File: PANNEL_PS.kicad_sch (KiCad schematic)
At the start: 24 parts, among them IC30 TPS25940ARVCR, IC31 INA226AIDGSR

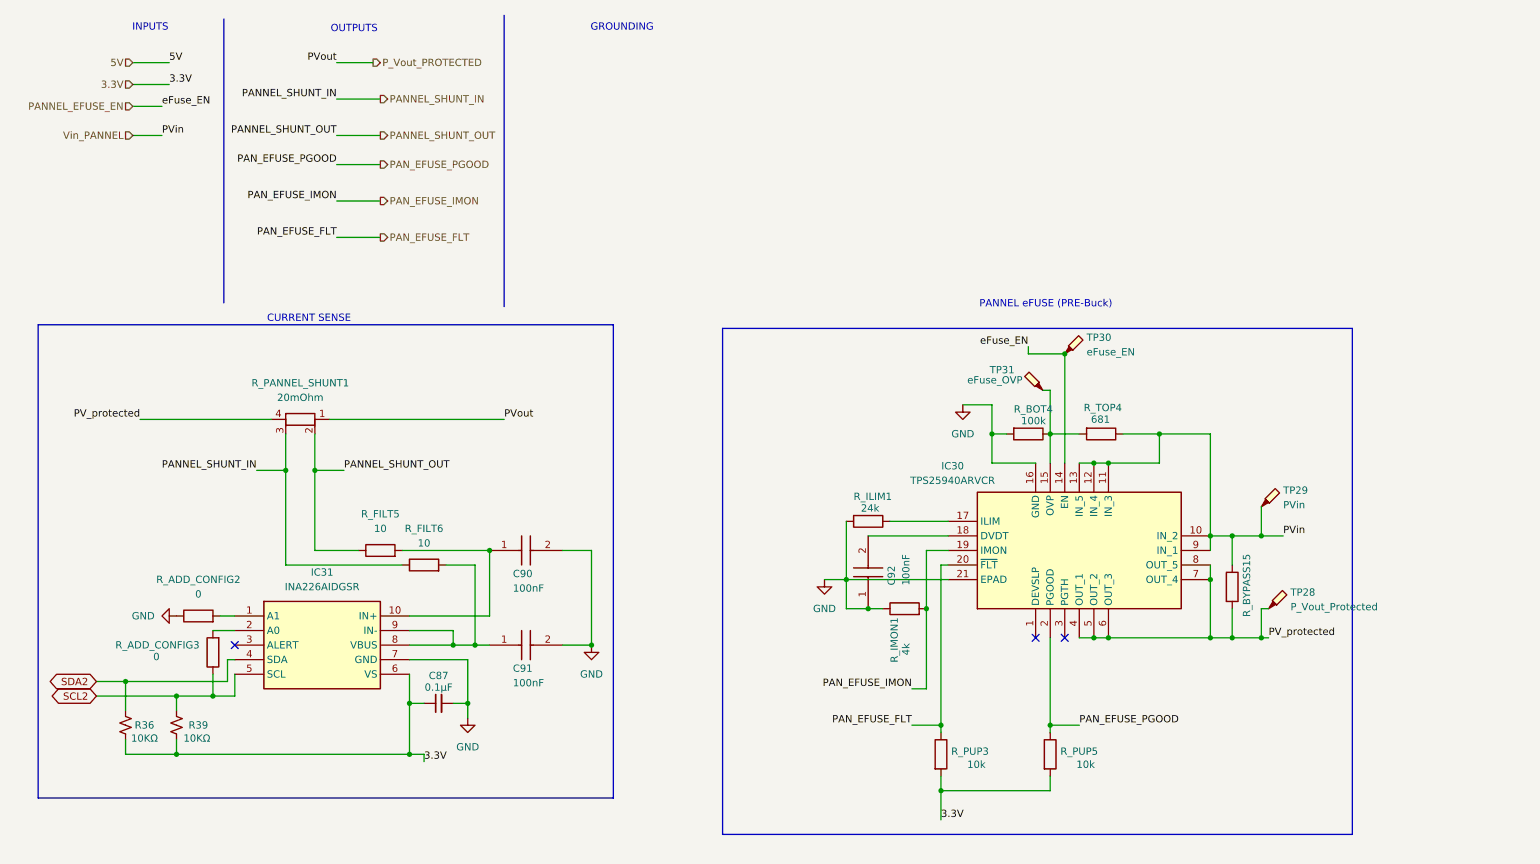
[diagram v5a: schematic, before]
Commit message: changed mcu power suppl
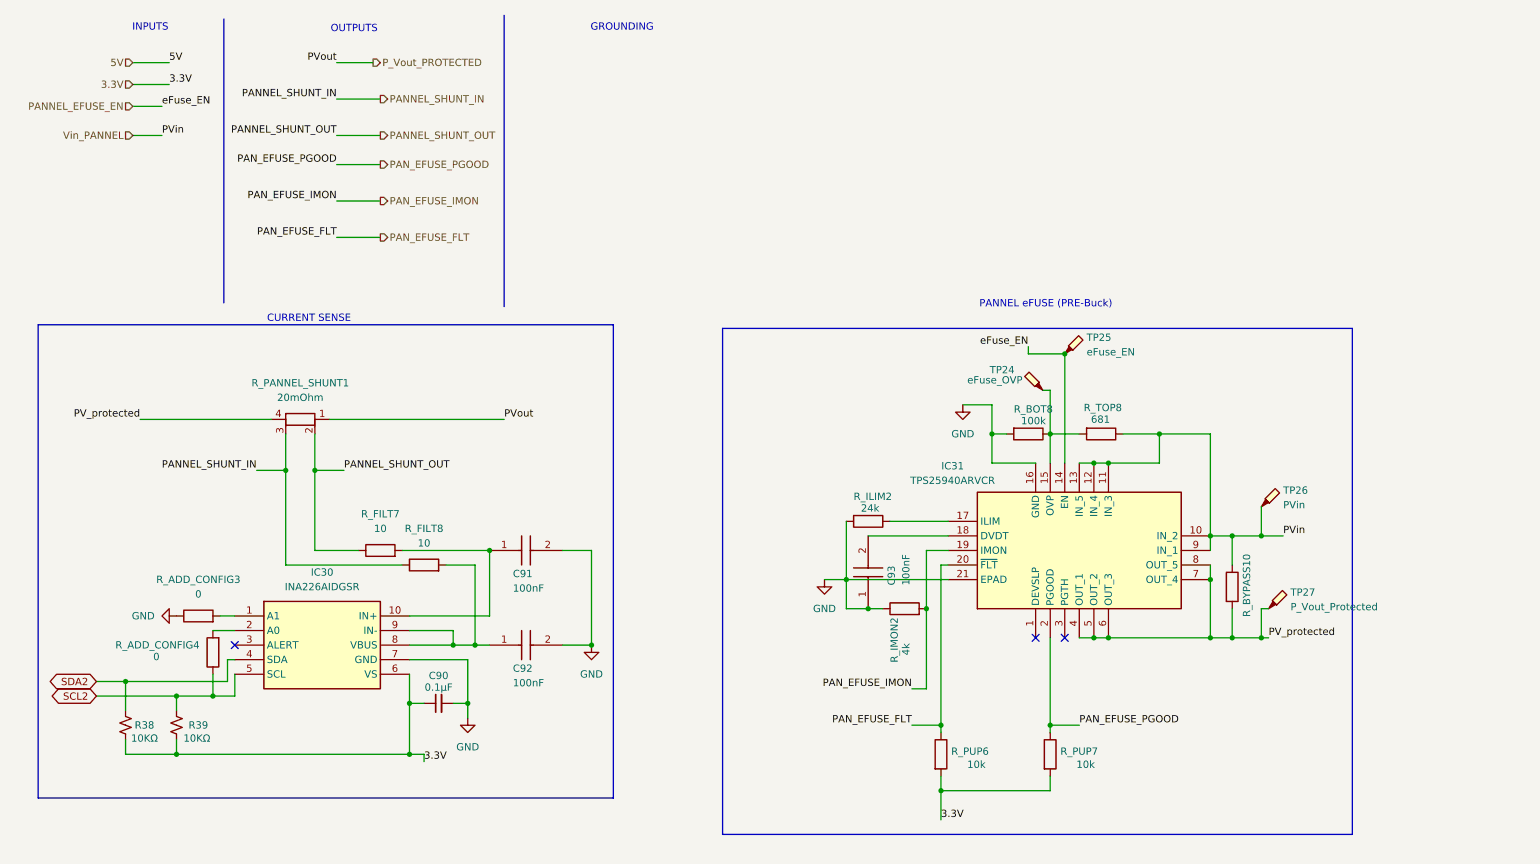
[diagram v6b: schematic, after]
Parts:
- renumbered C87 to C90, C90 to C91, C91 to C92, C92 to C93, IC31 to IC30, IC30 to IC31, R36 to R38, R_ADD_CONFIG2 to R_ADD_CONFIG3, R_ADD_CONFIG3 to R_ADD_CONFIG4, R_BOT4 to R_BOT8, R_BYPASS15 to R_BYPASS10, R_FILT5 to R_FILT7, R_FILT6 to R_FILT8, R_ILIM1 to R_ILIM2, R_IMON1 to R_IMON2, R_PUP3 to R_PUP6, R_PUP5 to R_PUP7, R_TOP4 to R_TOP8, TP31 to TP24, TP30 to TP25, TP29 to TP26, TP28 to TP27
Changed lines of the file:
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@@
 		(dnp no)
 		(fields_autoplaced yes)
-		(property "Reference" "IC31"
+		(property "Reference" "IC30"
 			(at 66.04 111.76 0)
 			(effects
@@
 			(project "PULSE_ENG"
 				(path "/2de881bb-2e2a-47f9-96ed-b3393fa36b98/c72bc6ca-9cdc-4e58-ad5e-fa33c03e7ecd"
-					(reference "IC31")
+					(reference "IC30")
 					(unit 1)
 				)
@@
 		(dnp no)
 		(fields_autoplaced yes)
-		(property "Reference" "#PWR025"
+		(property "Reference" "#PWR070"
 			(at 177.8 88.9 0)
 			(effects
@@
 			(project "PULSE_ENG"
 				(path "/2de881bb-2e2a-47f9-96ed-b3393fa36b98/c72bc6ca-9cdc-4e58-ad5e-fa33c03e7ecd"
-					(reference "#PWR025")
+					(reference "#PWR070")
 					(unit 1)
 				)
@@
 		(on_board yes)
 		(dnp no)
-		(property "Reference" "R_BOT4"
+		(property "Reference" "R_BOT8"
 			(at 186.69 83.312 90)
 			(effects
@@
 			(project "PULSE_ENG"
 				(path "/2de881bb-2e2a-47f9-96ed-b3393fa36b98/c72bc6ca-9cdc-4e58-ad5e-fa33c03e7ecd"
-					(reference "R_BOT4")
+					(reference "R_BOT8")
 					(unit 1)
 				)
@@
 		(on_board yes)
 		(dnp no)
-		(property "Reference" "R_PUP5"
+		(property "Reference" "R_PUP7"
 			(at 194.818 143.002 0)
 			(effects
@@
 			(project "PULSE_ENG"
 				(path "/2de881bb-2e2a-47f9-96ed-b3393fa36b98/c72bc6ca-9cdc-4e58-ad5e-fa33c03e7ecd"
-					(reference "R_PUP5")
+					(reference "R_PUP7")
 					(unit 1)
 				)
@@
 		(dnp no)
 		(fields_autoplaced yes)
-		(property "Reference" "#PWR024"
+		(property "Reference" "#PWR069"
 			(at 153.67 119.38 0)
 			(effects
@@
 			(project "PULSE_ENG"
 				(path "/2de881bb-2e2a-47f9-96ed-b3393fa36b98/c72bc6ca-9cdc-4e58-ad5e-fa33c03e7ecd"
-					(reference "#PWR024")
+					(reference "#PWR069")
 					(unit 1)
 				)
@@
 		(on_board yes)
 		(dnp no)
-		(property "Reference" "R_ILIM1"
+		(property "Reference" "R_ILIM2"
 			(at 158.75 98.552 90)
 			(effects
@@
 			(project "PULSE_ENG"
 				(path "/2de881bb-2e2a-47f9-96ed-b3393fa36b98/c72bc6ca-9cdc-4e58-ad5e-fa33c03e7ecd"
-					(reference "R_ILIM1")
+					(reference "R_ILIM2")
 					(unit 1)
 				)
@@
 		(dnp no)
 		(fields_autoplaced yes)
-		(property "Reference" "R_FILT6"
+		(property "Reference" "R_FILT8"
 			(at 83.82 104.14 90)
 			(effects
@@
 			(project "PULSE_ENG"
 				(path "/2de881bb-2e2a-47f9-96ed-b3393fa36b98/c72bc6ca-9cdc-4e58-ad5e-fa33c03e7ecd"
-					(reference "R_FILT6")
+					(reference "R_FILT8")
 					(unit 1)
 				)
@@
 		(on_board yes)
 		(dnp no)
-		(property "Reference" "IC30"
+		(property "Reference" "IC31"
 			(at 176.022 93.218 90)
 			(effects
@@
 			(project "PULSE_ENG"
 				(path "/2de881bb-2e2a-47f9-96ed-b3393fa36b98/c72bc6ca-9cdc-4e58-ad5e-fa33c03e7ecd"
-					(reference "IC30")
+					(reference "IC31")
 					(unit 1)
 				)
@@
 		(dnp no)
 		(fields_autoplaced yes)
-		(property "Reference" "R_FILT5"
+		(property "Reference" "R_FILT7"
 			(at 76.2 101.6 90)
 			(effects
@@
 			(project "PULSE_ENG"
 				(path "/2de881bb-2e2a-47f9-96ed-b3393fa36b98/c72bc6ca-9cdc-4e58-ad5e-fa33c03e7ecd"
-					(reference "R_FILT5")
+					(reference "R_FILT7")
 					(unit 1)
 				)
@@
 		(on_board yes)
 		(dnp no)
-		(property "Reference" "R_TOP4"
+		(property "Reference" "R_TOP8"
 			(at 198.882 83.058 90)
 			(effects
@@
 			(project "PULSE_ENG"
 				(path "/2de881bb-2e2a-47f9-96ed-b3393fa36b98/c72bc6ca-9cdc-4e58-ad5e-fa33c03e7ecd"
-					(reference "R_TOP4")
+					(reference "R_TOP8")
 					(unit 1)
 				)
@@
 		(on_board yes)
 		(dnp no)
-		(property "Reference" "TP31"
+		(property "Reference" "TP24"
 			(at 184.658 76.454 90)
 			(effects
@@
 			(project "PULSE_ENG"
 				(path "/2de881bb-2e2a-47f9-96ed-b3393fa36b98/c72bc6ca-9cdc-4e58-ad5e-fa33c03e7ecd"
-					(reference "TP31")
+					(reference "TP24")
 					(unit 1)
 				)
@@
 		(dnp no)
 		(fields_autoplaced yes)
-		(property "Reference" "#PWR021"
+		(property "Reference" "#PWR068"
 			(at 113.03 130.81 0)
 			(effects
@@
 			(project "PULSE_ENG"
 				(path "/2de881bb-2e2a-47f9-96ed-b3393fa36b98/c72bc6ca-9cdc-4e58-ad5e-fa33c03e7ecd"
-					(reference "#PWR021")
+					(reference "#PWR068")
 					(unit 1)
 				)
@@
 		(dnp no)
 		(fields_autoplaced yes)
-		(property "Reference" "TP29"
+		(property "Reference" "TP26"
 			(at 233.68 97.4724 0)
 			(effects
@@
 			(project "PULSE_ENG"
 				(path "/2de881bb-2e2a-47f9-96ed-b3393fa36b98/c72bc6ca-9cdc-4e58-ad5e-fa33c03e7ecd"
-					(reference "TP29")
+					(reference "TP26")
 					(unit 1)
 				)
@@
 		(dnp no)
 		(fields_autoplaced yes)
-		(property "Reference" "#PWR020"
+		(property "Reference" "#PWR067"
 			(at 91.44 143.51 0)
 			(effects
@@
 			(project "PULSE_ENG"
 				(path "/2de881bb-2e2a-47f9-96ed-b3393fa36b98/c72bc6ca-9cdc-4e58-ad5e-fa33c03e7ecd"
-					(reference "#PWR020")
+					(reference "#PWR067")
 					(unit 1)
 				)
@@
 		(on_board yes)
 		(dnp no)
-		(property "Reference" "R_PUP3"
+		(property "Reference" "R_PUP6"
 			(at 175.768 143.002 0)
 			(effects
@@
 			(project "PULSE_ENG"
 				(path "/2de881bb-2e2a-47f9-96ed-b3393fa36b98/c72bc6ca-9cdc-4e58-ad5e-fa33c03e7ecd"
-					(reference "R_PUP3")
+					(reference "R_PUP6")
 					(unit 1)
 				)
@@
 		(dnp no)
 		(fields_autoplaced yes)
-		(property "Reference" "#PWR019"
+		(property "Reference" "#PWR066"
 			(at 34.29 119.38 0)
 			(effects
@@
 			(project "PULSE_ENG"
 				(path "/2de881bb-2e2a-47f9-96ed-b3393fa36b98/c72bc6ca-9cdc-4e58-ad5e-fa33c03e7ecd"
-					(reference "#PWR019")
+					(reference "#PWR066")
 					(unit 1)
 				)
@@
 		(on_board yes)
 		(dnp no)
-		(property "Reference" "C90"
+		(property "Reference" "C91"
 			(at 99.314 112.014 0)
 			(effects
@@
 			(project "PULSE_ENG"
 				(path "/2de881bb-2e2a-47f9-96ed-b3393fa36b98/c72bc6ca-9cdc-4e58-ad5e-fa33c03e7ecd"
-					(reference "C90")
+					(reference "C91")
 					(unit 1)
 				)
@@
 		(dnp no)
 		(fields_autoplaced yes)
-		(property "Reference" "TP28"
+		(property "Reference" "TP27"
 			(at 234.95 115.2524 0)
 			(effects
@@
 			(project "PULSE_ENG"
 				(path "/2de881bb-2e2a-47f9-96ed-b3393fa36b98/c72bc6ca-9cdc-4e58-ad5e-fa33c03e7ecd"
-					(reference "TP28")
+					(reference "TP27")
 					(unit 1)
 				)
@@
 		(on_board yes)
 		(dnp no)
-		(property "Reference" "R_ADD_CONFIG3"
+		(property "Reference" "R_ADD_CONFIG4"
 			(at 29.972 124.46 0)
 			(effects
@@
 			(project "PULSE_ENG"
 				(path "/2de881bb-2e2a-47f9-96ed-b3393fa36b98/c72bc6ca-9cdc-4e58-ad5e-fa33c03e7ecd"
-					(reference "R_ADD_CONFIG3")
+					(reference "R_ADD_CONFIG4")
 					(unit 1)
 				)
@@
 		(on_board yes)
 		(dnp no)
-		(property "Reference" "C91"
+		(property "Reference" "C92"
 			(at 99.314 128.524 0)
 			(effects
@@
 			(project "PULSE_ENG"
 				(path "/2de881bb-2e2a-47f9-96ed-b3393fa36b98/c72bc6ca-9cdc-4e58-ad5e-fa33c03e7ecd"
-					(reference "C91")
+					(reference "C92")
 					(unit 1)
 				)
@@
 		(on_board yes)
 		(dnp no)
-		(property "Reference" "C92"
+		(property "Reference" "C93"
 			(at 165.354 114.046 0)
 			(effects
@@
 			(project "PULSE_ENG"
 				(path "/2de881bb-2e2a-47f9-96ed-b3393fa36b98/c72bc6ca-9cdc-4e58-ad5e-fa33c03e7ecd"
-					(reference "C92")
+					(reference "C93")
 					(unit 1)
 				)
@@
 		(dnp no)
 		(fields_autoplaced yes)
-		(property "Reference" "R_ADD_CONFIG2"
+		(property "Reference" "R_ADD_CONFIG3"
 			(at 44.45 113.03 90)
 			(effects
@@
 			(project "PULSE_ENG"
 				(path "/2de881bb-2e2a-47f9-96ed-b3393fa36b98/c72bc6ca-9cdc-4e58-ad5e-fa33c03e7ecd"
-					(reference "R_ADD_CONFIG2")
+					(reference "R_ADD_CONFIG3")
 					(unit 1)
 				)
@@
 		(on_board yes)
 		(dnp no)
-		(property "Reference" "R_BYPASS15"
+		(property "Reference" "R_BYPASS10"
 			(at 227.33 114.046 90)
 			(effects
@@
 			(project "PULSE_ENG"
 				(path "/2de881bb-2e2a-47f9-96ed-b3393fa36b98/c72bc6ca-9cdc-4e58-ad5e-fa33c03e7ecd"
-					(reference "R_BYPASS15")
+					(reference "R_BYPASS10")
 					(unit 1)
 				)
@@
 		(dnp no)
 		(fields_autoplaced yes)
-		(property "Reference" "TP30"
+		(property "Reference" "TP25"
 			(at 199.39 70.8024 0)
 			(effects
@@
 			(project "PULSE_ENG"
 				(path "/2de881bb-2e2a-47f9-96ed-b3393fa36b98/c72bc6ca-9cdc-4e58-ad5e-fa33c03e7ecd"
-					(reference "TP30")
+					(reference "TP25")
 					(unit 1)
 				)
@@
 		(on_board yes)
 		(dnp no)
-		(property "Reference" "C87"
+		(property "Reference" "C90"
 			(at 86.36 129.794 90)
 			(effects
@@
 			(project "PULSE_ENG"
 				(path "/2de881bb-2e2a-47f9-96ed-b3393fa36b98/c72bc6ca-9cdc-4e58-ad5e-fa33c03e7ecd"
-					(reference "C87")
+					(reference "C90")
 					(unit 1)
 				)
@@
 		(on_board yes)
 		(dnp no)
-		(property "Reference" "R_IMON1"
+		(property "Reference" "R_IMON2"
 			(at 165.862 127.508 0)
 			(effects
@@
 			(project "PULSE_ENG"
 				(path "/2de881bb-2e2a-47f9-96ed-b3393fa36b98/c72bc6ca-9cdc-4e58-ad5e-fa33c03e7ecd"
-					(reference "R_IMON1")
+					(reference "R_IMON2")
 					(unit 1)
 				)
@@
 		(on_board yes)
 		(dnp no)
-		(property "Reference" "R36"
+		(property "Reference" "R38"
 			(at 35.052 138.43 0)
 			(effects
@@
 			(project "PULSE_ENG"
 				(path "/2de881bb-2e2a-47f9-96ed-b3393fa36b98/c72bc6ca-9cdc-4e58-ad5e-fa33c03e7ecd"
-					(reference "R36")
-					(unit 1)
-				)
+					(reference "R38")
+					(unit 1)
+				)
